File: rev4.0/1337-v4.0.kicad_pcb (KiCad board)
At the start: 2 copper layers, 62 x 62 mm, 64 parts, among them J1 USB_IN, J2 AVR-ISP-6, SW1 SW_Push, SW2 EC11, U2 USBLC6-2SC6, U3 ATMEGA32U4, U5 SSD1306, Y2 16MHz

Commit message: traced PCB
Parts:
- removed C15, C16, C17, C21, C22, C26, C27: 100n, Capacitor_SMD:C_0603_1608Metric
- removed C18, C19: 22p, Capacitor_SMD:C_0603_1608Metric
- removed C20: 1u, Capacitor_SMD:C_0603_1608Metric
- removed D14: SK6812MINI-E, 0xcb:MX_SK6812MINI-E
- removed R14, R7: 10k, Resistor_SMD:R_0603_1608Metric
- removed RN2: 10k, Resistor_SMD:R_Array_Convex_4x0603
- removed SW2: EC11, Rotary_Encoder:RotaryEncoder_Alps_EC11E-Switch_Vertical_H20mm
- removed U5: SSD1306, 0xcb:128x64OLED
- removed Y2: 16MHz, 0xcb:Crystal_SMD_3225-4Pin_3.2x2.5mm
- removed svg2mod: G***, svg2mod
- added D8: SK6812MINI-E, 0xcb:MX_SK6812MINI-E, F.Cu at (126.6, 84.4)
- added MX9: MX, 0xcb:SW_Cherry_MX_PCB_1.00u, F.Cu at (126.6, 84.4)
- added R1: 5.1k, Resistor_SMD:R_0603_1608Metric, B.Cu at (122.3, 42.5)
- added R4: 22, Resistor_SMD:R_0603_1608Metric, B.Cu at (115.5, 50.2)
- added RN1: 10k, Resistor_SMD:R_Array_Convex_4x0603, B.Cu at (129.2, 46.3)
- added U1: SSD1306, 0xcb:128x64OLED, F.Cu at (90.0, 46.7)
- added Y1: 16MHz, 0xcb:Crystal_SMD_3225-4Pin_3.2x2.5mm, B.Cu at (119.9, 69.0)
- C1, C10, C12, C14, C4, C6, C7, C8, F1, FB1, FB2, J1, J2, R2, SW1, U2, U3: moved to B.Cu
- C11: value 1u -> 22p; moved to B.Cu
- C13: value 100n -> 22p; moved to B.Cu
- C2: value 1u -> 100n; moved to B.Cu
- C3, C5, C9: value 100n -> 1u; moved to B.Cu
- D1, D2, D3, D4: value WS2812B -> SK6812MINI-E; footprint LED_SMD:LED_WS2812B_PLCC4_5.0x5.0mm_P3.2mm -> 0xcb:MX_SK6812MINI-E
- D10, D11, D12, D13: value SK6812MINI-E -> WS2812B; footprint 0xcb:MX_SK6812MINI-E -> LED_SMD:LED_WS2812B_PLCC4_5.0x5.0mm_P3.2mm; moved to B.Cu
- D5: value SMF5.0CA -> SK6812MINI-E; footprint Diode_SMD:D_SOD-123F -> 0xcb:MX_SK6812MINI-E
- D9: value SK6812MINI-E -> SMF5.0CA; footprint 0xcb:MX_SK6812MINI-E -> Diode_SMD:D_SOD-123F; moved to B.Cu
- MX3: value MX -> EC11; footprint 0xcb:SW_Cherry_MX_PCB_1.00u -> 0xcb:EC11
- R3: value 5.1k -> 22; moved to B.Cu
- R5, R6: value 22 -> 10k; moved to B.Cu
- moved C14 215.1 mm to (77.8, 89.4), turned to -90 degrees
- moved C12 211.4 mm to (77.8, 70.4), turned to -90 degrees
- moved MX4 185.5 mm to (82.4, 65.3)
- moved D6 183.9 mm to (82.4, 84.4)
- moved J2 168.5 mm to (126.1, 55.7)
- moved D13 166.5 mm to (91.9, 74.9)
- moved SW1 166.0 mm to (114.0, 90.9), turned to 180 degrees
- moved C1 162.3 mm to (109.1, 44.4)
- moved MX1 158.5 mm to (82.4, 46.3)
- moved C2 155.6 mm to (126.8, 44.8), turned to 90 degrees
- moved FB1 153.2 mm to (110.9, 39.6), turned to -90 degrees
- moved D4 151.1 mm to (101.4, 65.3)
- moved D1 150.8 mm to (82.4, 46.3)
- moved C9 149.0 mm to (118.1, 59.4)
- moved C5 147.7 mm to (109.2, 49.0), turned to 180 degrees
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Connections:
- C11 pad 1: VCC -> GND
- C11 pad 2: GND -> Net-(C11-Pad2)
- C13 pad 1: VCC -> GND
- C13 pad 2: GND -> Net-(C13-Pad2)
- C2 pad 1: VCC -> EB
- C4 pad 1: VCC -> EA
- C9 pad 1: VCC -> Net-(C9-Pad1)
- D1 pad 2: Net-(D1-Pad2) -> Net-(D5-Pad4)
- D1 pad 4: RGB -> Net-(D11-Pad2)
- D10 pad 4: Net-(D10-Pad4) -> RGB
- D11 pad 4: Net-(D10-Pad2) -> Net-(D11-Pad4)
- D12 pad 2: unconnected-(D12-Pad2) -> Net-(D4-Pad4)
- D12 pad 4: Net-(D12-Pad4) -> Net-(D5-Pad2)
- D13 pad 2: Net-(D12-Pad4) -> Net-(D13-Pad2)
- D13 pad 4: Net-(D13-Pad4) -> Net-(D4-Pad2)
- D2 pad 2: Net-(D2-Pad2) -> Net-(D11-Pad4)
- D2 pad 4: Net-(D1-Pad2) -> Net-(D10-Pad2)
- D3 pad 2: Net-(D3-Pad2) -> Net-(D8-Pad4)
- D3 pad 4: Net-(D2-Pad2) -> Net-(D13-Pad2)
- D4 pad 4: Net-(D3-Pad2) -> Net-(D4-Pad4)
- D5 pad 1: GND -> VCC
- D5 pad 2: Net-(C1-Pad1) -> Net-(D5-Pad2)
- D6 pad 2: Net-(D6-Pad2) -> unconnected-(D6-Pad2)
- D7 pad 4: Net-(D4-Pad2) -> Net-(D7-Pad4)
- D9 pad 1: VCC -> GND
- D9 pad 2: Net-(D10-Pad4) -> Net-(C1-Pad1)
- FB1 pad 1: Net-(C1-Pad1) -> GND
- FB1 pad 2: VCC -> Net-(FB1-Pad2)
- FB2 pad 1: GND -> Net-(C1-Pad1)
- FB2 pad 2: Net-(FB2-Pad2) -> VCC
- J1 pad S1: Net-(FB2-Pad2) -> Net-(FB1-Pad2)
- J2 pad 1: S6 -> EA
- J2 pad 3: S5 -> S3
- J2 pad 4: S9 -> EB
- MX4 pad 2: S5 -> S4
- MX5 pad 2: S6 -> S5
- MX6 pad 2: S7 -> S6
- MX7 pad 2: S8 -> S7
- MX8 pad 2: S9 -> S8
- R3 pad 1: GND -> /MCU+
- R3 pad 2: Net-(J1-PadB5) -> D+
- R5 pad 1: /MCU+ -> RST
- R5 pad 2: D+ -> VCC
- R6 pad 1: /MCU- -> GND
- R6 pad 2: D- -> Net-(R6-Pad2)
- U3 pad 1: S7 -> unconnected-(U3-Pad1)
- U3 pad 10: S9 -> EB
- U3 pad 11: S6 -> EA
- U3 pad 12: unconnected-(U3-Pad12) -> S6
- U3 pad 16: Net-(C18-Pad2) -> Net-(C11-Pad2)
- U3 pad 17: Net-(C19-Pad2) -> Net-(C13-Pad2)
- U3 pad 20: S1 -> unconnected-(U3-Pad20)
- U3 pad 21: RGB -> unconnected-(U3-Pad21)
- U3 pad 25: S2 -> S9
- U3 pad 26: unconnected-(U3-Pad26) -> S8
- U3 pad 27: S4 -> S7
- U3 pad 28: S8 -> S4
- U3 pad 29: unconnected-(U3-Pad29) -> S5
- U3 pad 30: unconnected-(U3-Pad30) -> S1
- U3 pad 31: unconnected-(U3-Pad31) -> S2
- U3 pad 33: Net-(R14-Pad2) -> Net-(R6-Pad2)
- U3 pad 37: EB -> unconnected-(U3-Pad37)
- U3 pad 38: EA -> unconnected-(U3-Pad38)
- U3 pad 39: S3 -> unconnected-(U3-Pad39)
- U3 pad 6: Net-(C20-Pad1) -> Net-(C9-Pad1)
- U3 pad 8: unconnected-(U3-Pad8) -> RGB
- U3 pad 9: S5 -> S3
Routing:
- net VCC: track 0.00 -> 392.7 mm, vias 0 -> 11
- net RST: track 0.00 -> 78.7 mm
- net Net-(D5-Pad4): track 0.00 -> 60.0 mm
- net Net-(D8-Pad4): track 0.00 -> 57.1 mm
- net SCL: track 0.00 -> 51.7 mm, vias 0 -> 1
- net SDA: track 0.00 -> 50.7 mm, vias 0 -> 1
- net S1: track 0.00 -> 39.0 mm, vias 0 -> 1
- net S4: track 0.00 -> 33.1 mm, vias 0 -> 1
- net S7: track 0.00 -> 32.9 mm, vias 0 -> 1
- net S2: track 0.00 -> 28.7 mm, vias 0 -> 1
- net S3: track 0.00 -> 28.2 mm, vias 0 -> 1
- net EB: track 0.00 -> 26.7 mm
- net S9: track 0.00 -> 23.2 mm, vias 0 -> 1
- net /VBUS: track 0.00 -> 22.8 mm, vias 0 -> 3
- net EA: track 0.00 -> 22.7 mm, vias 0 -> 1
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- added copper zone on B.Cu, net GND
- added copper zone on F.Cu, net GND
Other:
- outline, holes or cut-outs redrawn
- board text removed: "v3.0"

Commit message: rounded traces, added logo etc
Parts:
- added G***: LOGO, 0xcb:CB-sm, B.Cu at (111.8, 81.8)
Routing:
- net VCC: track 392.7 -> 401.9 mm
- net S9: track 23.2 -> 27.1 mm
- net S4: track 33.1 -> 30.3 mm
- net S8: track 16.1 -> 18.1 mm
- net /VBUS: track 22.8 -> 24.5 mm
- net EA: track 22.7 -> 24.2 mm
- net Net-(D12-Pad4): track 7.15 -> 8.37 mm
- net S5: track 14.2 -> 13.0 mm
- net EB: track 26.7 -> 27.8 mm
- net Net-(D1-Pad2): track 60.0 -> 59.0 mm
- net RST: track 78.7 -> 77.8 mm
- net Net-(D13-Pad2): track 5.96 -> 6.66 mm
- net Net-(D1-Pad4): track 5.96 -> 6.66 mm
- net GND: vias 7 -> 12
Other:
- outline, holes or cut-outs redrawn

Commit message: prod push
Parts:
- added REF**: OSHW-Logo2_7.3x6mm_SilkScreen, Symbol:OSHW-Logo2_7.3x6mm_SilkScreen, F.Cu at (91.9, 85.3)
- added REF**: OSHW-Logo2_7.3x6mm_SilkScreen, Symbol:OSHW-Logo2_7.3x6mm_SilkScreen, B.Cu at (91.9, 85.2)
- added kibuzzard-61BA68AC: G***, kibuzzard-61BA68AC, F.Cu at (111.5, 86.8)
- added kibuzzard-61BA68AC: G***, kibuzzard-61BA68AC, B.Cu at (112.2, 86.8)
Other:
- board text added: "ISP"
- board text added: "RST"
- board text added: "rev 4.0"

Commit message: finalizing v4.0
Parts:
- removed the REF** at (91.9, 85.3)
- removed the REF** at (91.9, 85.2)
- added REF**: Tab, kikit:Tab, F.Cu at (104.5, 96.6)
- added REF**: Tab, kikit:Tab, F.Cu at (104.5, 34.1)
- added REF**: Tab, kikit:Tab, F.Cu at (135.7, 65.3)
- added REF**: Tab, kikit:Tab, F.Cu at (73.2, 65.3)
- added REF**: OSHW-Symbol_6.7x6mm_SilkScreen, Symbol:OSHW-Symbol_6.7x6mm_SilkScreen, F.Cu at (91.9, 81.8)
- added REF**: OSHW-Symbol_6.7x6mm_SilkScreen, Symbol:OSHW-Symbol_6.7x6mm_SilkScreen, B.Cu at (91.9, 81.8)
- moved kibuzzard-61BA68AC 0.07 mm to (111.5, 86.8)
- moved kibuzzard-61BA68AC 0.07 mm to (112.2, 86.8)
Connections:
- J2 pad 1: EA -> MISO
- J2 pad 3: S3 -> SCK / S3
- J2 pad 4: EB -> MOSI
- U3 pad 10: EB -> MOSI
- U3 pad 11: EA -> MISO
- U3 pad 18: SDA -> SCL
- U3 pad 19: SCL -> SDA
- U3 pad 40: unconnected-(U3-Pad40) -> EA
- U3 pad 41: unconnected-(U3-Pad41) -> EB
- U3 pad 9: S3 -> SCK / S3
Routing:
- net S3: track 28.3 -> 0.00 mm, vias 1 -> 0
- net SCK / S3: track 0.00 -> 28.0 mm, vias 0 -> 1
- net MISO: track 0.00 -> 13.1 mm, vias 0 -> 1
- net MOSI: track 0.00 -> 12.4 mm
- net EA: track 24.2 -> 29.8 mm, vias 1 -> 2
- net EB: track 27.8 -> 31.2 mm, vias 0 -> 2
- net SDA: track 50.8 -> 49.4 mm
- net /VBUS: track 24.5 -> 25.7 mm
- net SCL: track 51.9 -> 50.7 mm
- net GND: vias 12 -> 23
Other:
- board text added: "v4.0"
- board text removed: "rev 4.0"

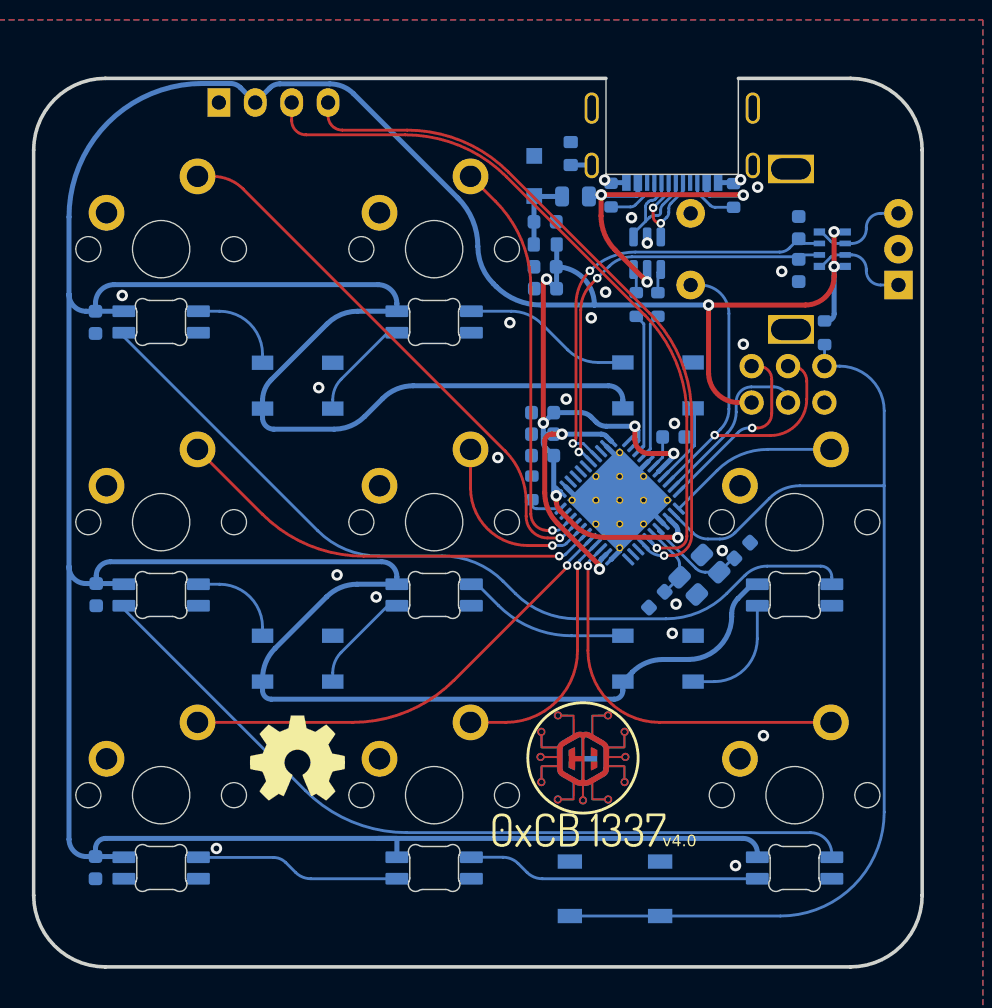
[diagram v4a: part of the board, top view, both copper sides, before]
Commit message: added teardrops
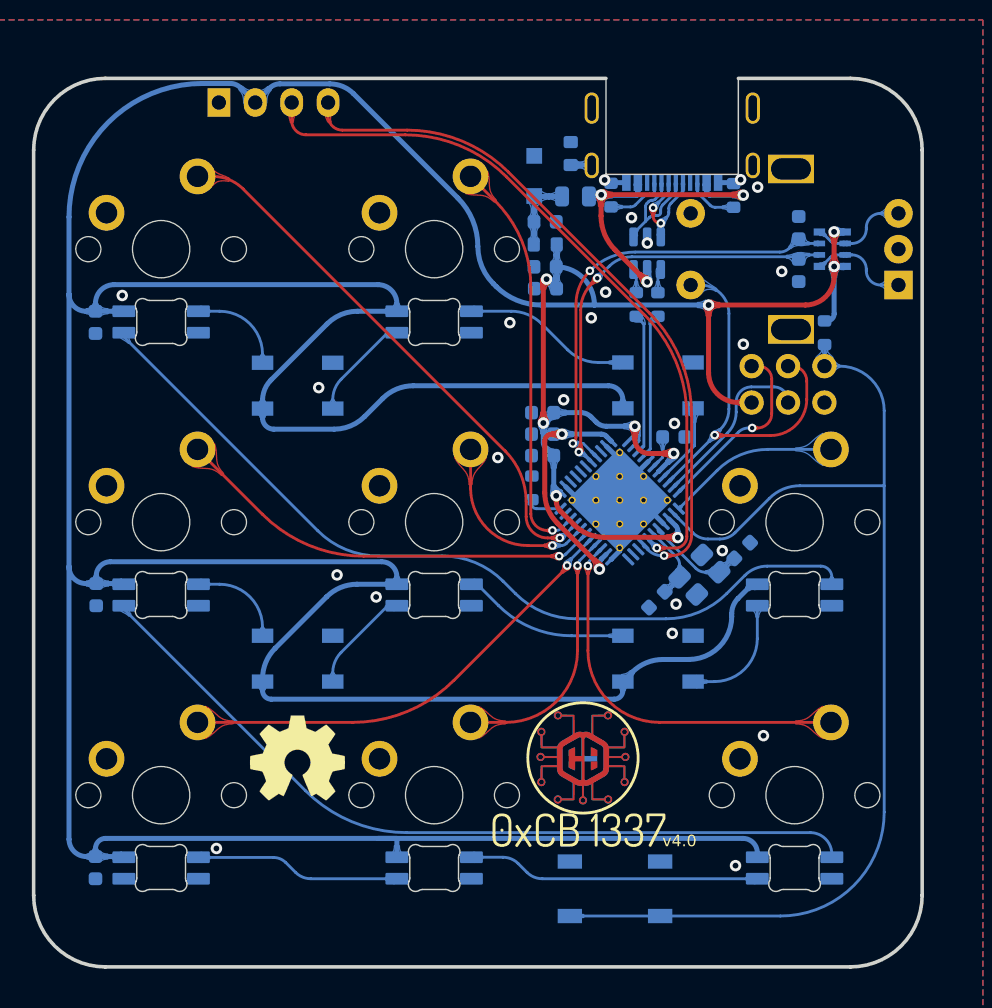
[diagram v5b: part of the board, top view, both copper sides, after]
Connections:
- J2 pad 3: SCK / S3 -> S3
- U3 pad 9: SCK / S3 -> S3
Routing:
- net SCK / S3: track 28.0 -> 0.00 mm, vias 1 -> 0
- net S3: track 0.00 -> 28.0 mm, vias 0 -> 1
